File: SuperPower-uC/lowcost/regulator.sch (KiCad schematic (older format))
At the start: 0 parts

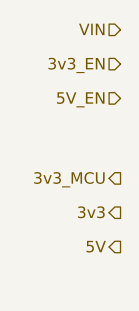
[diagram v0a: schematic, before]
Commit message: int pins and charging module
added Interrupt pins to the main sheet and finished the charging module sub sheet (with charger, fuel Gauge and power on int)
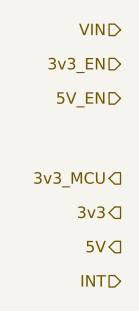
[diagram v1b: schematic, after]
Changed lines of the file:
@@
 Text HLabel 1150 1450 0    50   Output ~ 0
 3v3_MCU
+Text HLabel 1150 1900 0    50   Input ~ 0
+INT
 $EndSCHEMATC

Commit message: io expander, rtc cirquit, i2c pullup...
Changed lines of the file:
@@
 $EndDescr
 Text HLabel 1150 800  0    50   Input ~ 0
-VIN
+VBAT
 Text HLabel 1150 1600 0    50   Output ~ 0
 3v3

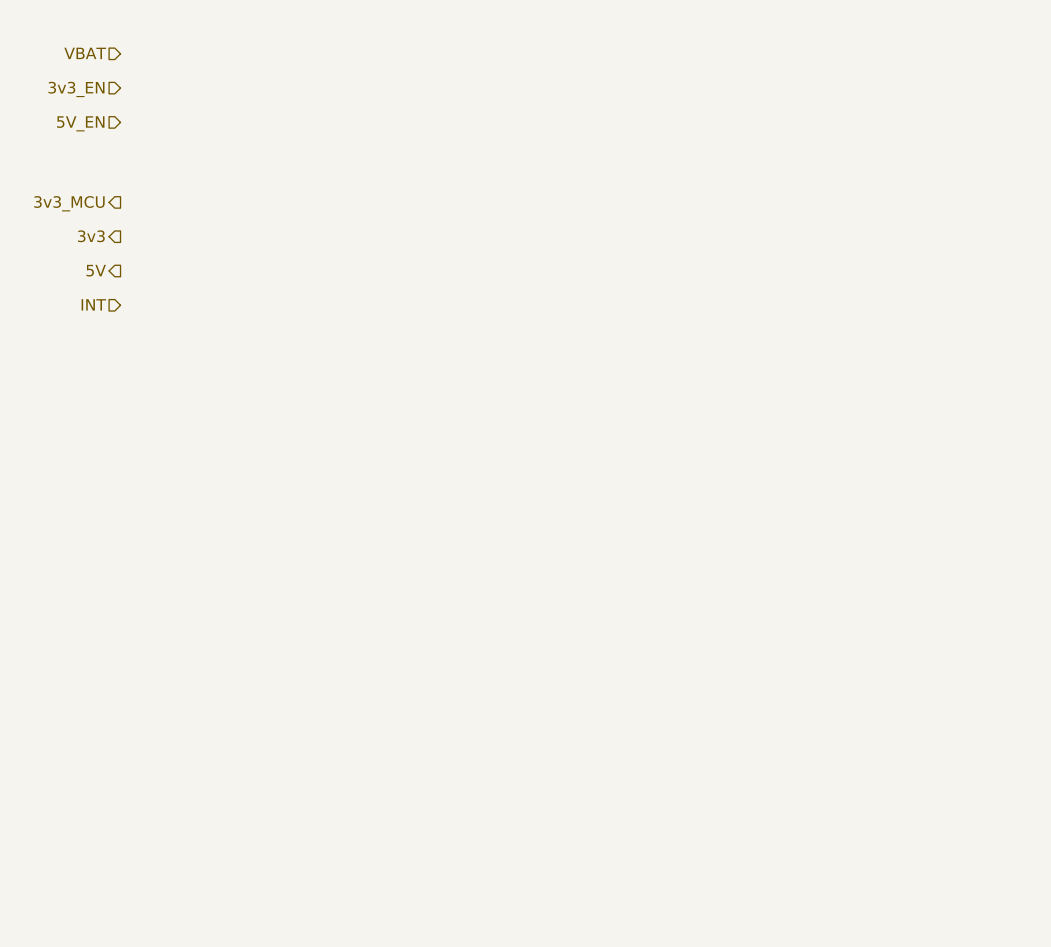
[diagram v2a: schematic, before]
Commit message: naming fixes, more components and continued schematics
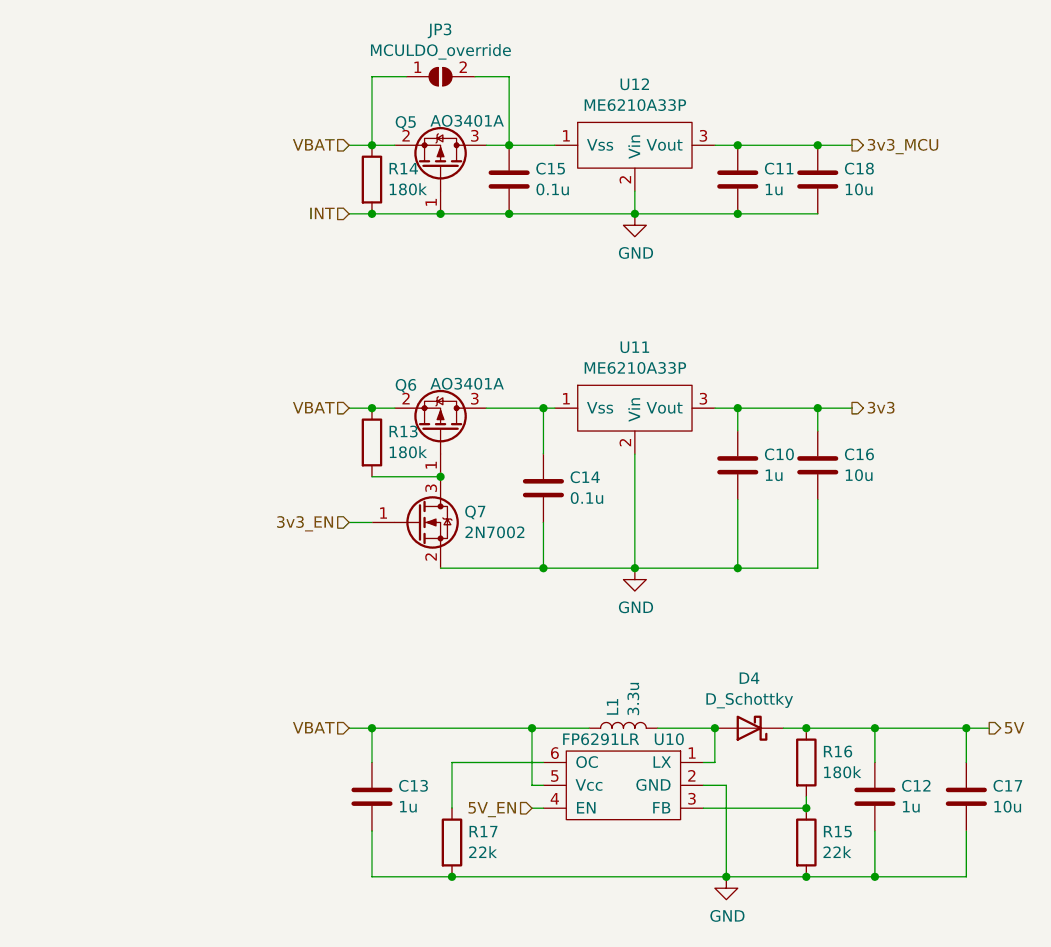
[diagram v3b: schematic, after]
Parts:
- added C10, C11, C12, C13: 1u, Capacitor_SMD:C_0603_1608Metric_Pad1.05x0.95mm_HandSolder, symbol Device:C
- added C14, C15: 0.1u, Capacitor_SMD:C_0603_1608Metric_Pad1.05x0.95mm_HandSolder, symbol Device:C
- added C16, C17, C18: 10u, Capacitor_SMD:C_0603_1608Metric_Pad1.05x0.95mm_HandSolder, symbol Device:C
- added D4: D_Schottky, Diode_SMD:D_SMA_Handsoldering, symbol Device:D_Schottky
- added JP3: MCULDO_override, Jumper:SolderJumper-2_P1.3mm_Open_Pad1.0x1.5mm, symbol Jumper:SolderJumper_2_Open
- added L1: 3.3u, Inductor_SMD:L_0805_2012Metric_Pad1.15x1.40mm_HandSolder, symbol Device:L
- added Q5, Q6: AO3401A, Package_TO_SOT_SMD:SOT-23_Handsoldering, symbol Transistor_FET:AO3401A
- added Q7: 2N7002, Package_TO_SOT_SMD:SOT-23, symbol Transistor_FET:2N7002
- added R13, R14, R16: 180k, Resistor_SMD:R_0603_1608Metric_Pad1.05x0.95mm_HandSolder, symbol Device:R
- added R15, R17: 22k, Resistor_SMD:R_0603_1608Metric_Pad1.05x0.95mm_HandSolder, symbol Device:R
- added U10: FP6291LR, Package_TO_SOT_SMD:SOT-23-6_Handsoldering, symbol FP6291LR:FP6291LR
- added U11, U12: ME6210A33P, Package_TO_SOT_SMD:SOT-89-3_Handsoldering, symbol ME6210A33P:ME6210A33P
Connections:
- net 3v3: now also C10.1, C16.1, U11.3 (Vout)
- net 3v3_EN: now also Q7.1 (G)
- net 3v3_MCU: now also C11.1, C18.1, U12.3 (Vout)
- net 5V: now also C12.1, C17.1, D4.1 (K), R16.1
- net 5V_EN: now also U10.4 (EN)
- net VBAT: now also C13.1, JP3.1 (A), L1.1, Q5.2 (S), Q6.2 (S), R13.1, R14.1, U10.5 (Vcc)
- new net: D4.2 (A), L1.2, U10.1 (LX)
- new net: R15.1, R16.2, U10.3 (FB)
- new net: R17.1, U10.6 (OC)
- new net: C15.1, JP3.2 (B), Q5.3 (D), U12.1 (Vss)
- new net: C14.1, Q6.3 (D), U11.1 (Vss)
- new net: Q6.1 (G), Q7.3 (D), R13.2
- new net GND: C10.2, C11.2, C12.2, C13.2, C14.2, C15.2, C16.2, C17.2, C18.2, Q5.1 (G), Q7.2 (S), R14.2, R15.2, R17.2, U10.2 (GND), U11.2 (Vin), U12.2 (Vin)

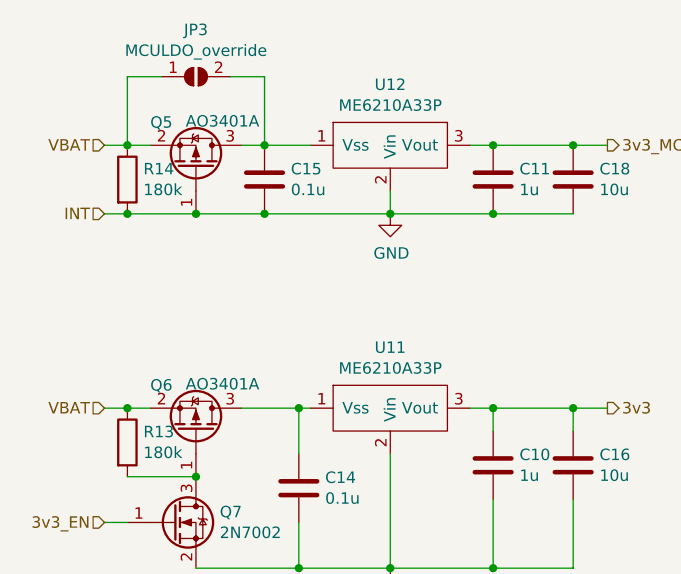
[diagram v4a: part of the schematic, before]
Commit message: fixed erc errors
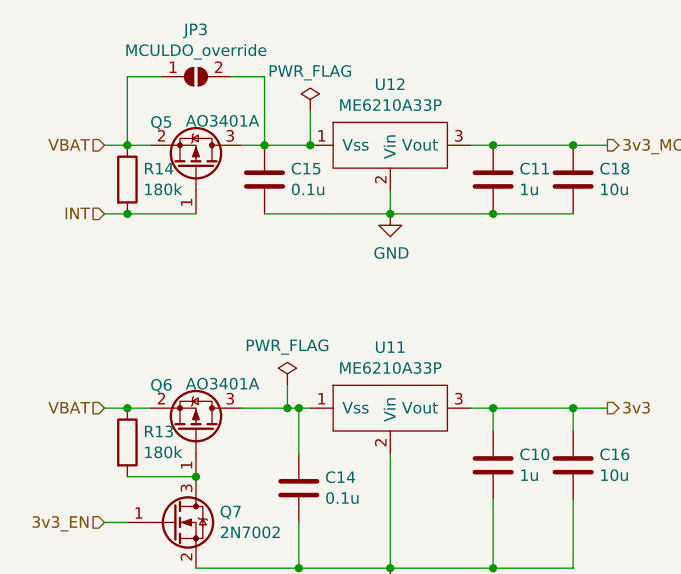
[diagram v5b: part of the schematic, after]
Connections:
- net GND: no longer Q5.1 (G), R14.2
- new net INT: Q5.1 (G), R14.2
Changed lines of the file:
@@
 	2750 1200 2850 1200
 Wire Wire Line
-	2750 2350 3000 2350
+	2750 2350 2950 2350
 $Comp
 L Device:R R13
@@
 Wire Wire Line
 	3400 1400 3400 1500
-Wire Wire Line
-	2550 1500 2850 1500
-Connection ~ 2550 1500
 Connection ~ 3400 1500
 Wire Wire Line
@@
 Wire Wire Line
 	2850 1200 3050 1200
-Connection ~ 2850 1500
 Wire Wire Line
 	2850 1500 3400 1500
@@
 Text HLabel 4950 3750 2    50   Output ~ 0
 5V
+$Comp
+L power:PWR_FLAG #FLG0105
+U 1 1 5F875FD2
+P 2950 2250
+F 0 "#FLG0105" H 2950 2325 50  0001 C CNN
+F 1 "PWR_FLAG" H 2950 2423 50  0000 C CNN
+F 2 "" H 2950 2250 50  0001 C CNN
+F 3 "~" H 2950 2250 50  0001 C CNN
+	1    2950 2250
+	1    0    0    -1
+$EndComp
+Wire Wire Line
+	2950 2250 2950 2350
+Connection ~ 2950 2350
+Wire Wire Line
+	2950 2350 3000 2350
+$Comp
+L power:PWR_FLAG #FLG0106
+U 1 1 5F877C10
+P 3050 1050
+F 0 "#FLG0106" H 3050 1125 50  0001 C CNN
+F 1 "PWR_FLAG" H 3050 1223 50  0000 C CNN
+F 2 "" H 3050 1050 50  0001 C CNN
+F 3 "~" H 3050 1050 50  0001 C CNN
+	1    3050 1050
+	1    0    0    -1
+$EndComp
+Wire Wire Line
+	3050 1050 3050 1200
+Connection ~ 3050 1200
 $EndSCHEMATC

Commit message: design rule optimisation
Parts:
- C10, C11, C12, C13: value 1u -> 1µF
- C14, C15: value 0.1u -> 0.1µF
- C16, C17, C18: value 10u -> 10µF
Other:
- moved on the sheet: C10, C11, C14, C15, C16, C18, JP3, Q5, Q6, Q7, R13, U11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

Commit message: schematic layout cleaning
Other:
- note added: "3.3V Sensor Regulator\n"
- note added: "5V Sensor Regulator"
- note added: "MCU 3.3v Regulator\n"
- note added: "labels\n"
- moved on the sheet: C10, C11, C12, C13, C14, C15, C16, C17, C18, D4, JP3, L1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
